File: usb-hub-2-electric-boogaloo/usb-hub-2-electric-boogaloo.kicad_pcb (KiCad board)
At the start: 2 copper layers, 54.8 x 25 mm, 40 parts, among them U1 SL2.1S, U2 GL823K-HCY04

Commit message: some (bad) routing
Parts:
- moved D2 16.1 mm to (135.4, 72.4), turned to -90 degrees
- moved C7 10.5 mm to (122.8, 66.1)
- moved C6 10.5 mm to (123.4, 64.5)
- moved C5 9.77 mm to (133.1, 66.0)
- moved C4 9.77 mm to (133.1, 64.4)
- moved C10 6.71 mm to (123.2, 70.9)
- moved C9 6.71 mm to (124.7, 70.9)
- moved C15 4.32 mm to (130.8, 71.4)
- moved R10 3.47 mm to (92.8, 82.0)
- moved R9 3.19 mm to (90.0, 83.6)
- moved R8 2.51 mm to (89.4, 82.0)
- moved R6 2.22 mm to (90.7, 66.2)
- moved R7 2.22 mm to (92.2, 66.2)
- moved R3 1.65 mm to (105.7, 76.2)
- moved R4 1.65 mm to (116.7, 76.2)
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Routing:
- net GND: track 0.00 -> 66.0 mm, vias 0 -> 1
- net +5V: track 0.00 -> 38.4 mm
- net SD_CMD: track 0.00 -> 9.47 mm
- net D3: track 0.00 -> 8.76 mm
- net Net-(D2-K): track 0.00 -> 8.26 mm
- net Net-(U2-VDD): track 0.00 -> 7.68 mm
- net D0: track 0.00 -> 5.66 mm
- net D2: track 0.00 -> 5.40 mm
- net D1: track 0.00 -> 4.09 mm
- net Net-(USB1-CC2): track 0.00 -> 4.01 mm
- net Net-(USB2-CC1): track 0.00 -> 3.84 mm
- net Net-(USB1-CC1): track 0.00 -> 3.82 mm
- net Net-(USB2-CC2): track 0.00 -> 2.36 mm
- added copper zone on B.Cu, net GND

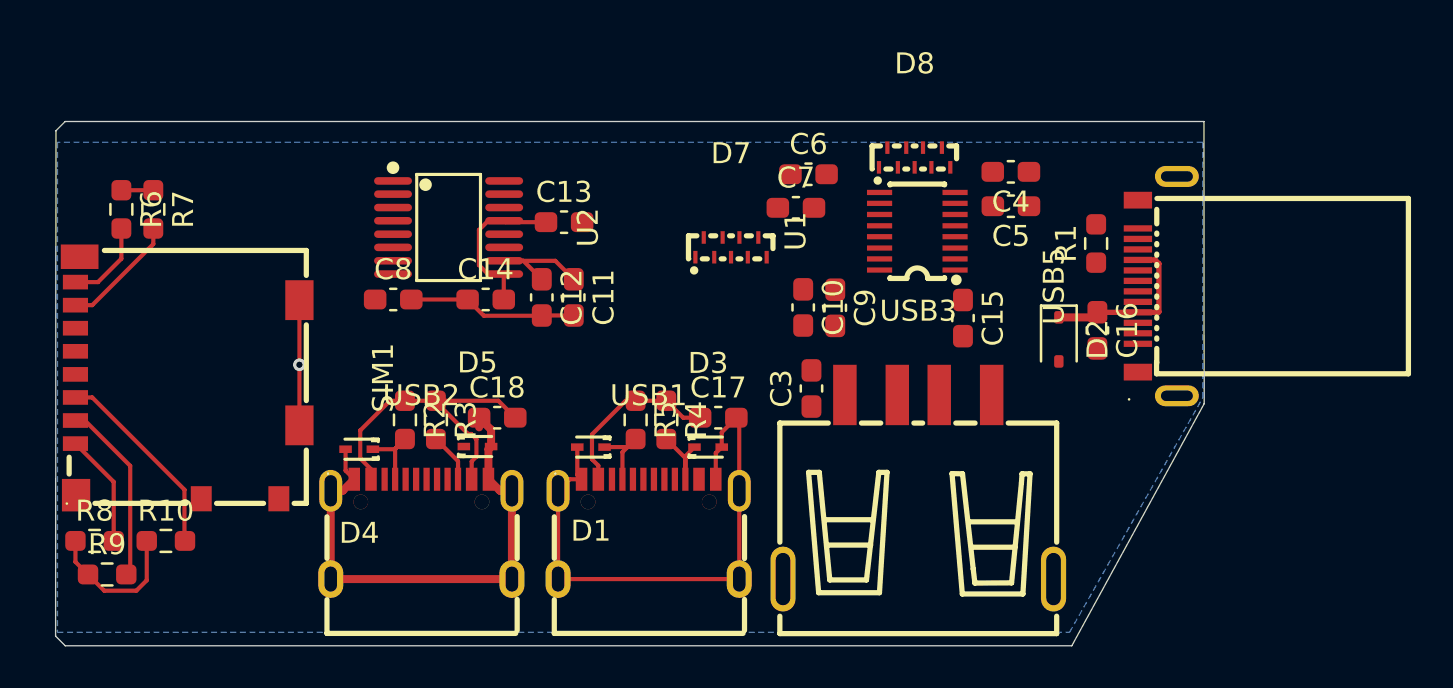
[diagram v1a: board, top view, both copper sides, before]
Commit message: routing traces
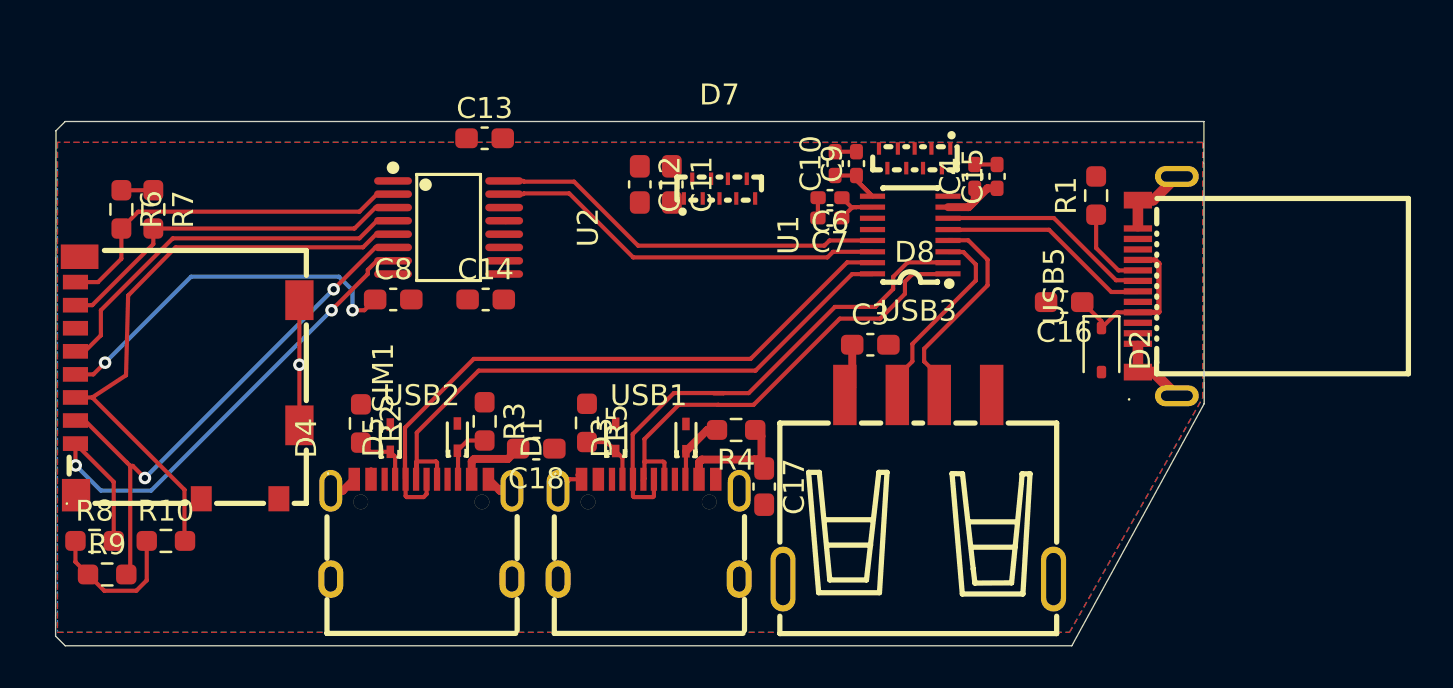
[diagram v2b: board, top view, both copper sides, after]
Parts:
- removed C5: 1u, Capacitor_SMD:C_0603_1608Metric_Pad1.08x0.95mm_HandSolder
- C10, C15, C4, C6, C7, C9: footprint Capacitor_SMD:C_0603_1608Metric_Pad1.08x0.95mm_HandSolder -> Capacitor_SMD:C_0402_1005Metric_Pad0.74x0.62mm_HandSolder
- moved C11 7.13 mm to (116.9, 65.0)
- moved C12 7.13 mm to (115.4, 65.0)
- moved C10 7.03 mm to (124.7, 64.0), turned to 90 degrees
- moved C9 6.95 mm to (125.7, 64.0), turned to 90 degrees
- moved C15 6.95 mm to (132.4, 64.6), turned to 90 degrees
- moved C13 5.51 mm to (108.0, 62.8)
- moved C17 3.95 mm to (121.3, 79.4), turned to -90 degrees
- moved C3 3.50 mm to (126.4, 72.6), turned to 0 degrees
- moved R4 3.36 mm to (120.0, 76.7), turned to 180 degrees
- moved D7 2.85 mm to (119.2, 65.2)
- moved C18 2.38 mm to (110.5, 77.6), turned to 180 degrees
- moved R5 2.32 mm to (112.9, 76.4)
- moved R3 2.32 mm to (108.0, 76.3)
- moved R1 2.29 mm to (137.2, 65.5)
- moved R2 2.11 mm to (102.1, 76.4)
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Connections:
- net DM1 renamed D1-
- net DM4 renamed D4-
- net DP1 renamed D1+
- net DP4 renamed D4+
- D8 pad 1: DP2 -> D2+
- D8 pad 2: DM2 -> D2-
- D8 pad 4: DP3 -> D3+
- D8 pad 5: DM3 -> D3-
- U1 pad 1: DM2 -> D2+
- U1 pad 15: DM3 -> D3-
- U1 pad 16: DP3 -> D3+
- U1 pad 2: DP2 -> D2-
- USB1 pad A6: DP3 -> D2+
- USB1 pad A7: DM3 -> D2-
- USB1 pad B6: DP3 -> D2+
- USB1 pad B7: DM3 -> D2-
- USB2 pad A6: DP2 -> D3+
- USB2 pad A7: DM2 -> D3-
- USB2 pad B6: DP2 -> D3+
- USB2 pad B7: DM2 -> D3-
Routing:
- net GND: track 66.0 -> 20.5 mm
- net D3-: track 0.00 -> 31.7 mm
- net D3+: track 0.00 -> 30.6 mm
- net D2-: track 0.00 -> 24.2 mm
- net D2+: track 0.00 -> 21.8 mm
- net D2: track 5.40 -> 26.7 mm, vias 0 -> 2
- net SD_CMD: track 9.47 -> 29.1 mm
- net D4+: track 0.00 -> 19.0 mm
- net D4-: track 0.00 -> 18.9 mm
- net SD_CLK: track 0.00 -> 18.4 mm
- net PMOS: track 0.00 -> 17.7 mm, vias 0 -> 2
- net D3: track 8.76 -> 26.1 mm, vias 0 -> 2
- net D1: track 4.09 -> 17.7 mm
- net +5V: track 38.4 -> 25.5 mm
- net D0: track 5.66 -> 17.5 mm
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- added copper zone on F.Cu, net +5V

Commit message: finish main routing (still disconnects tho)
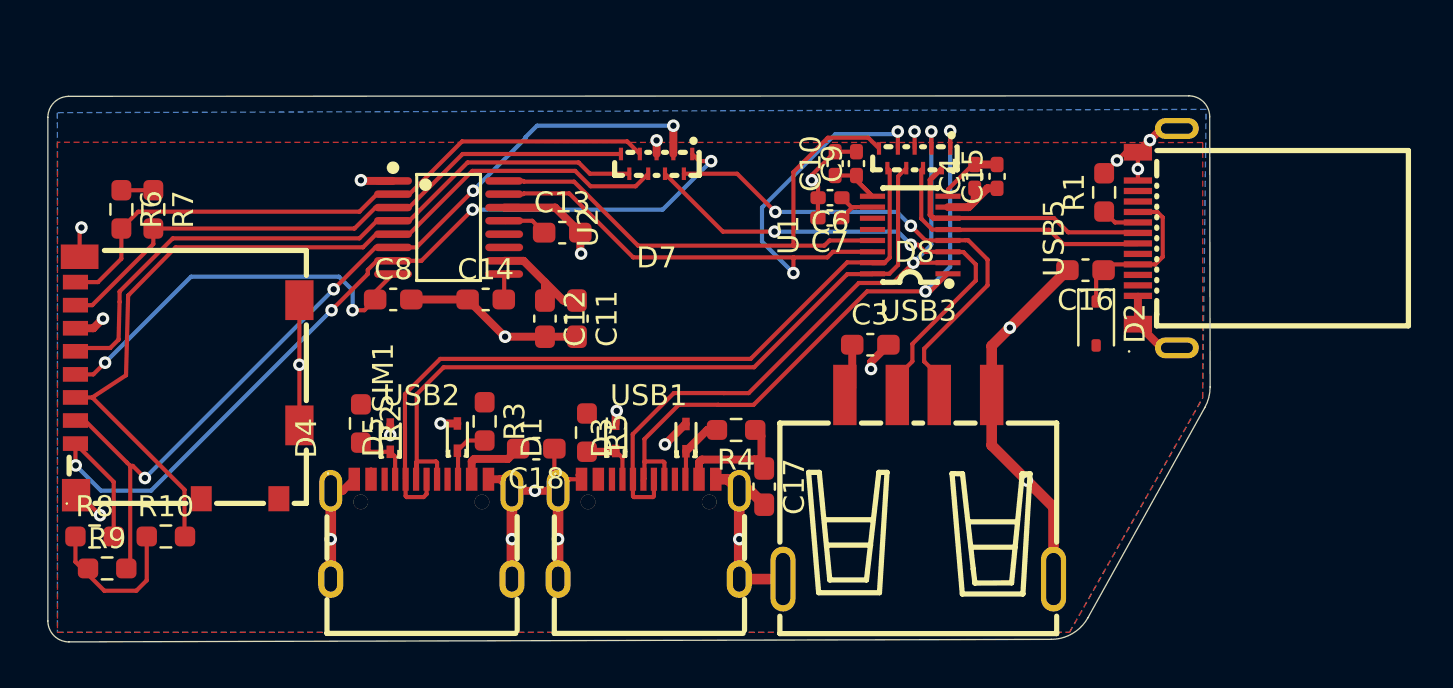
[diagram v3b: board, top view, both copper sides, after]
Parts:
- moved C11 7.84 mm to (112.4, 71.4)
- moved C12 7.84 mm to (110.9, 71.4)
- moved C13 5.83 mm to (111.7, 67.3)
- moved D7 3.22 mm to (116.2, 64.0), turned to 180 degrees
- moved USB5 2.29 mm to (140.1, 67.6)
- moved C16 1.83 mm to (136.7, 69.1)
- moved D2 1.30 mm to (137.2, 71.6)
- moved R5 0.46 mm to (112.9, 76.8)
- moved R1 0.41 mm to (137.5, 65.4)
- moved R9 0.29 mm to (90.0, 83.3)
- moved R10 0.21 mm to (92.8, 81.8)
- moved R8 0.21 mm to (89.4, 81.8)
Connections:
- D7 pad 1: D0 -> D2
- D7 pad 2: D1 -> D3
- D7 pad 4: D2 -> D1
- D7 pad 5: D3 -> D0
- D7 pad 8: D1+ -> D1-
- D7 pad 9: D1- -> D1+
- D8 pad 4: D3+ -> D4+
- D8 pad 5: D3- -> D4-
- D8 pad 6: D4+ -> D3-
- D8 pad 7: D4- -> D3+
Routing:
- net GND: track 20.5 -> 97.5 mm, vias 1 -> 25
- net D2: track 26.7 -> 44.7 mm, vias 2 -> 4
- net D3: track 26.1 -> 43.2 mm, vias 2 -> 4
- net D1-: track 9.35 -> 24.4 mm, vias 0 -> 2
- net D1+: track 11.7 -> 25.7 mm, vias 0 -> 2
- net SD_CMD: track 29.1 -> 42.8 mm
- net SD_CLK: track 18.4 -> 32.1 mm
- net D4+: track 19.0 -> 32.1 mm, vias 0 -> 2
- net D1: track 17.7 -> 30.8 mm
- net D0: track 17.5 -> 29.4 mm
- net D2+: track 21.8 -> 30.5 mm, vias 0 -> 2
- net D4-: track 18.9 -> 27.4 mm
- net D3+: track 30.6 -> 37.0 mm
- net D2-: track 24.2 -> 30.2 mm, vias 0 -> 2
- net +5V: track 25.5 -> 31.2 mm
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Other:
- board size 54.8 x 25 mm -> 55.4 x 26 mm

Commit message: vias and mounting holes
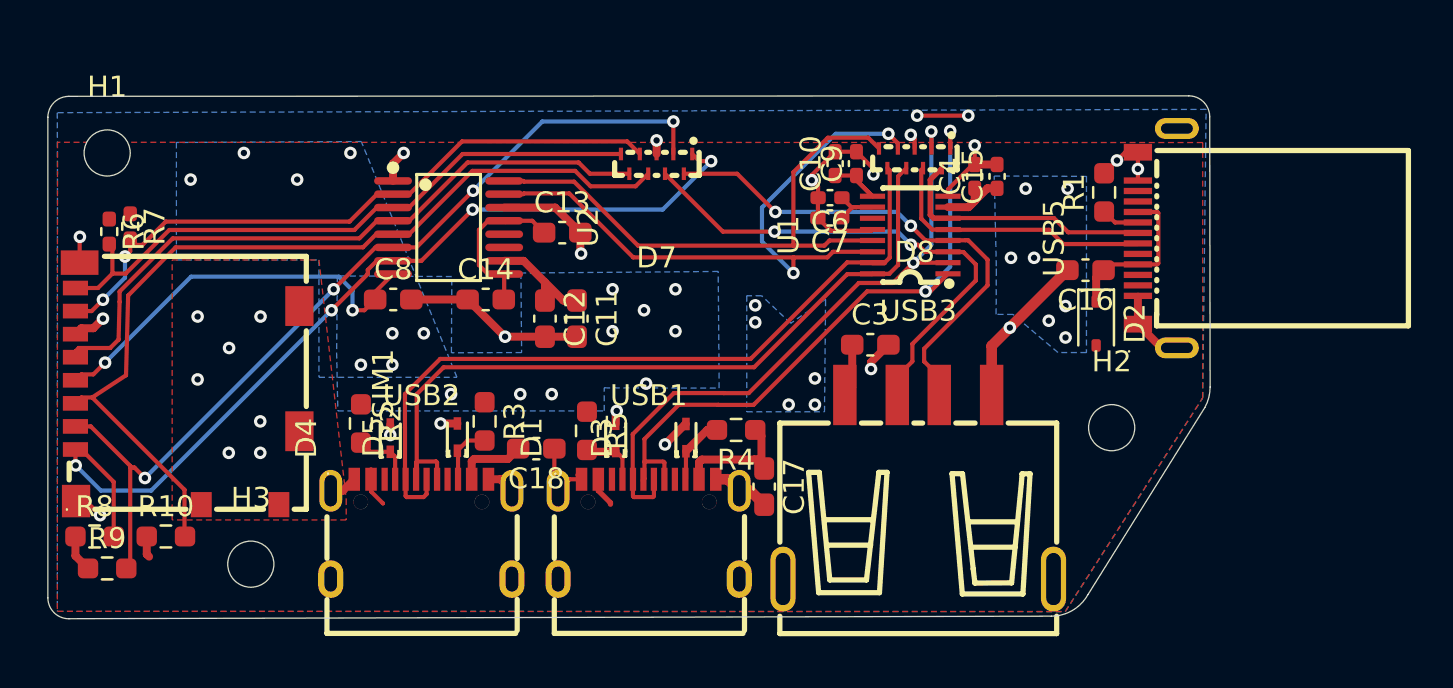
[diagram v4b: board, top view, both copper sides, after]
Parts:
- added H1: MountingHole, MountingHole:MountingHole_2.2mm_M2, F.Cu at (90.0, 63.5)
- added H2: MountingHole, MountingHole:MountingHole_2.2mm_M2, F.Cu at (137.9, 76.6)
- added H3: MountingHole, MountingHole:MountingHole_2.2mm_M2, F.Cu at (96.9, 83.1)
- R6, R7: footprint Resistor_SMD:R_0603_1608Metric_Pad0.98x0.95mm_HandSolder -> Resistor_SMD:R_0402_1005Metric_Pad0.72x0.64mm_HandSolder
- moved R7 1.37 mm to (91.1, 67.0)
- moved R6 1.21 mm to (90.1, 67.2)
- moved SIM1 0.28 mm to (93.8, 74.5)
- moved R5 0.08 mm to (112.9, 76.8)
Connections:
- D7 pad 4: D1 -> D0
- D7 pad 5: D0 -> D1
- U2 pad 2: D1 -> D0
- U2 pad 3: D0 -> D1
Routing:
- net GND: track 97.5 -> 66.3 mm, vias 25 -> 28
- net +5V: track 31.2 -> 28.2 mm, vias 0 -> 29
- net Net-(U2-VDD): track 5.02 -> 7.92 mm
- net D1: track 30.8 -> 29.4 mm
- net D0: track 29.4 -> 30.5 mm, vias 0 -> 2
- added copper zone on B.Cu, net +5V
- added copper zone on F.Cu, net GND
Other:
- board size 55.4 x 26 mm -> 55.4 x 24.9 mm

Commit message: whoops drc exists
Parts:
- moved C3 0.76 mm to (126.8, 72.0)
- moved USB3 0.68 mm to (128.7, 78.8)
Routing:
- net GND: track 66.3 -> 65.3 mm
- net +5V: track 28.2 -> 28.4 mm, vias 29 -> 32

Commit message: dxf + fixed 3D view + silkscreen
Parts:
- added G***: LOGO, LOGO, F.Cu at (118.6, 69.9)
- added G***: LOGO, LOGO, B.Cu at (93.3, 80.6)
- added G***: LOGO, LOGO, B.Cu at (115.6, 82.5)
- added G***: LOGO, LOGO, B.Cu at (132.1, 78.1)
- added G***: LOGO, LOGO, B.Cu at (133.0, 68.8)
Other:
- board text added: "Another USB Hub SL2.1S Micro SD 2x USB-C 1x USB-A USB-C Receptacle (no need for another cable *cough cough*)"
- board text added: "Made by @obob for Fallout! (hack.af/fallout) 2026-06-08 23:36 AEDT (Y-M-D)"
- board text added: "REV.1"
- board text added: "USBH: EB2"
- board text added: "a usb hub! made by @obob"

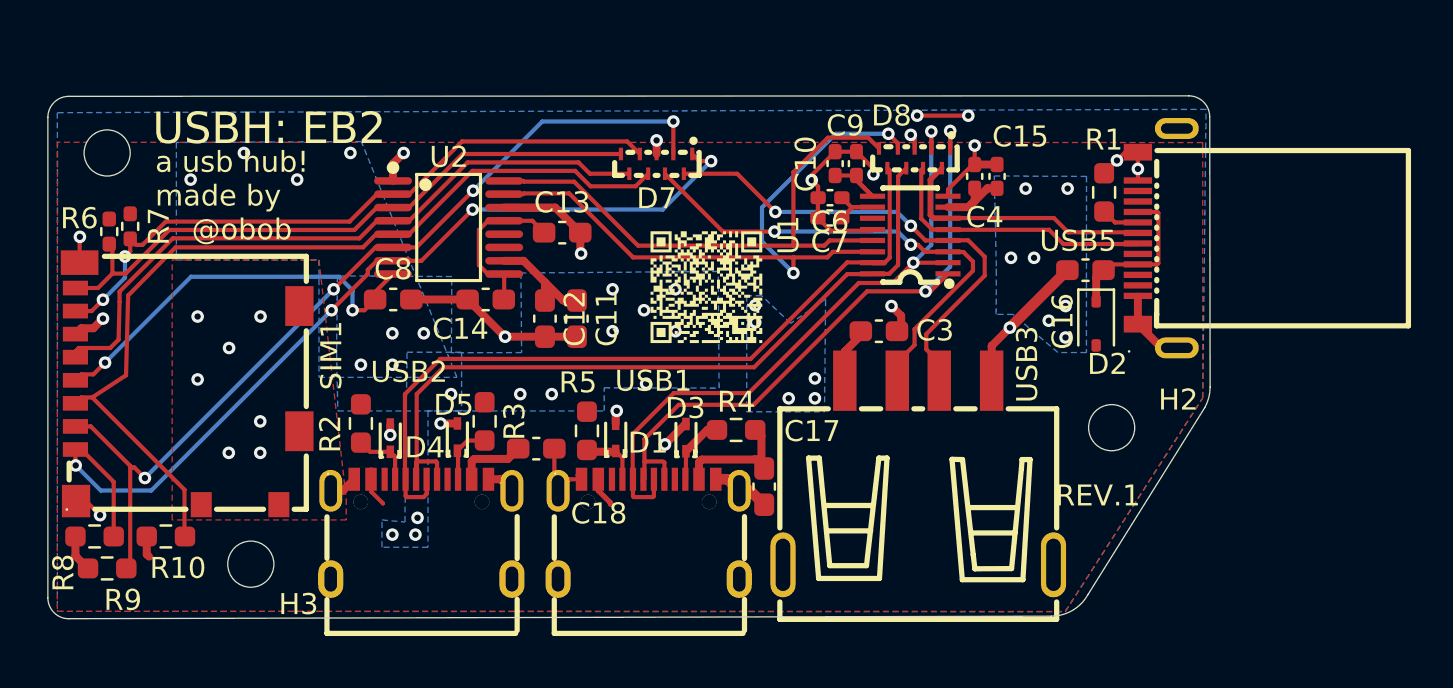
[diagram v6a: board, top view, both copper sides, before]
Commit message: zine + cad case + renders
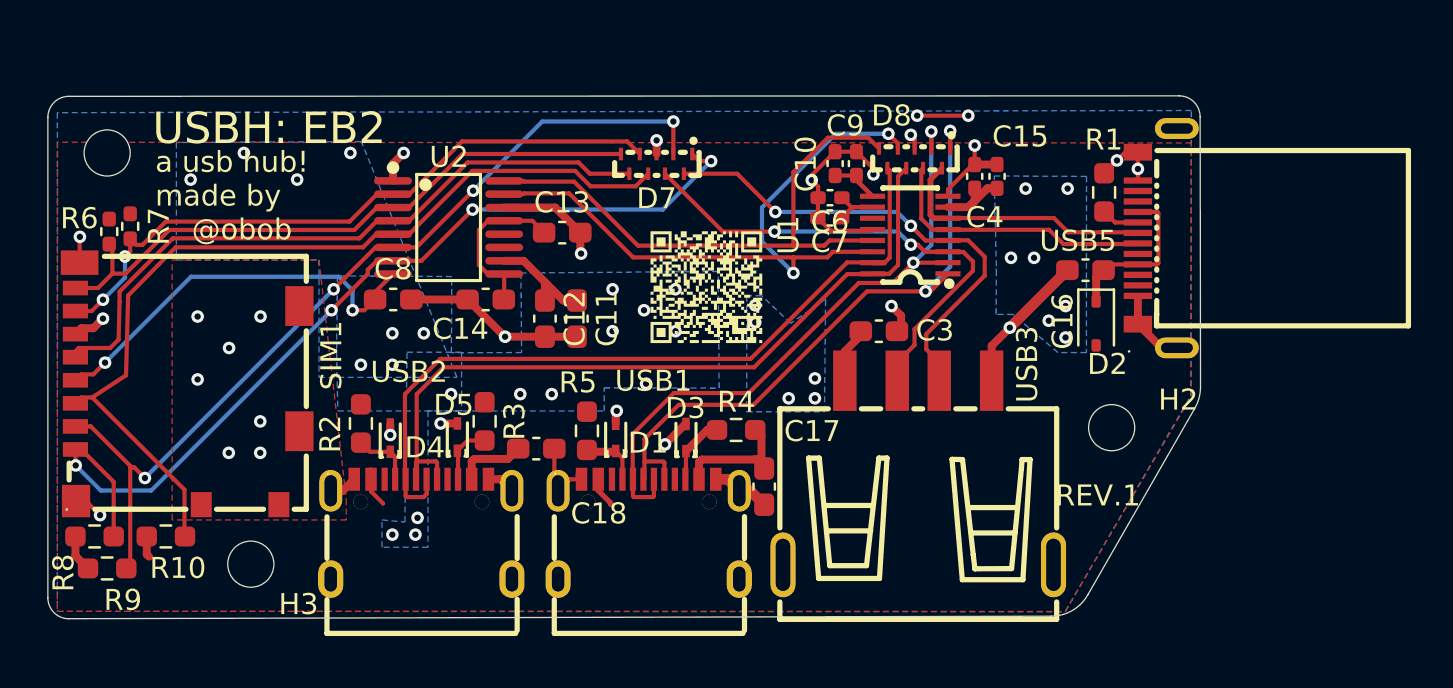
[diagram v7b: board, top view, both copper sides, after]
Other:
- board size 55.4 x 24.9 mm -> 55 x 24.9 mm
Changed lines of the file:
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@@
 	(gr_line
 		(start 136.76937 84.560733)
-		(end 142.342656 75.638729)
+		(end 141.886516 75.638729)
 		(stroke
 			(width 0.05)
@@
 	)
 	(gr_line
-		(start 141.575982 60.775447)
+		(start 141.118145 60.775447)
 		(end 88.172353 60.799331)
 		(stroke
@@
 	)
 	(gr_arc
-		(start 141.575982 60.775447)
-		(mid 142.282837 61.06769)
-		(end 142.576428 61.774017)
+		(start 141.118145 60.775447)
+		(mid 141.82497 61.067719)
+		(end 142.118591 61.774017)
 		(stroke
 			(width 0.05)
@@
 		(layer "Edge.Cuts")
 	)
-	(gr_arc
-		(start 142.594856 74.663656)
-		(mid 142.53114 75.167328)
-		(end 142.342656 75.638729)
+	(gr_line
+		(start 142.137656 74.663656)
+		(end 142.119228 61.774017)
 		(stroke
 			(width 0.05)
@@
 		(layer "Edge.Cuts")
 	)
-	(gr_line
-		(start 142.594856 74.663656)
-		(end 142.576428 61.774017)
+	(gr_arc
+		(start 142.138716 74.663656)
+		(mid 142.074995 75.167326)
+		(end 141.886516 75.638729)
 		(stroke
 			(width 0.05)
@@
 		(hatch edge 0.5)
 		(priority 1)
-		(connect_pads
+		(connect_pads thru_hole_only
 			(clearance 0.5)
 		)
@@
 		(polygon
 			(pts
-				(xy 142.243012 63.00351) (xy 87.63 62.99) (xy 87.623462 85.35535) (xy 135.6868 85.3694) (xy 142.24 75.18)
+				(xy 141.7 63.025) (xy 87.63 62.99) (xy 87.623462 85.35535) (xy 135.6868 85.3694) (xy 141.7 75.1)
 			)
 		)
@@
 		(polygon
 			(pts
-				(xy 87.624758 85.357456) (xy 135.6868 85.3694) (xy 142.24 75.184) (xy 142.403314 61.420722) (xy 87.622238 61.579206)
+				(xy 87.624758 85.357456) (xy 135.6868 85.3694) (xy 141.675 75.075) (xy 141.7 61.475) (xy 87.622238 61.579206)
 				(xy 87.63 64.262)
 			)

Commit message: fix usb + new renders
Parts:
- removed USB5: GT-USB-8016B, easyeda2kicad:USB-SMD_GT-USB-8016B
- added USB1: TYPE-C 16PIN 2MD, easyeda2kicad:USB-C-SMD_TYPE-C-16PIN-2MD-073, F.Cu at (138.5, 68.0)
- R4: renamed from R1; footprint Resistor_SMD:R_0603_1608Metric_Pad0.98x0.95mm_HandSolder -> Resistor_SMD:R_0402_1005Metric_Pad0.72x0.64mm_HandSolder
- moved R4 8.19 mm to (138.6, 73.5), turned to 180 degrees
- moved D1 7.45 mm to (134.8, 64.6), turned to 90 degrees
- moved C2 3.31 mm to (134.3, 71.4), turned to -90 degrees
- renumbered C8 to C1, C9 to C10, C7 to C11, C6 to C12, C3 to C13, C17 to C14, C18 to C15, C16 to C2, C14 to C3, C13 to C4, C12 to C5, C11 to C6, C15 to C7, C4 to C8, C10 to C9, D2 to D1, D7 to D2, D8 to D3, D1 to D4, D3 to D5, D4 to D6, D5 to D7, R10 to R1, R2 to R10, R9 to R2, R8 to R3, R6 to R5, R7 to R6, R4 to R7, R5 to R8, R3 to R9, U2 to U1, U1 to U2, USB3 to USB2, USB1 to USB3, USB2 to USB4
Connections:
- net Net-(D2-K) renamed /VBUS_D
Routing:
- net GND: track 65.3 -> 59.6 mm, vias 28 -> 26
- net Net-(USB1-CC1): track 1.83 -> 5.97 mm
- net /VBUS_D: track 7.78 -> 9.62 mm, vias 0 -> 2
- net D+: track 12.7 -> 11.7 mm
- net D-: track 13.3 -> 12.6 mm
- net +5V: vias 32 -> 29
